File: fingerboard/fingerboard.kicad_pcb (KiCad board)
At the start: 2 copper layers, 15 x 75.5 mm, 8 parts, among them J1 Conn_01x05_Pin, SW1 SW_Push, SW2 SW_Push, SW3 SW_Push, SW4 SW_Push

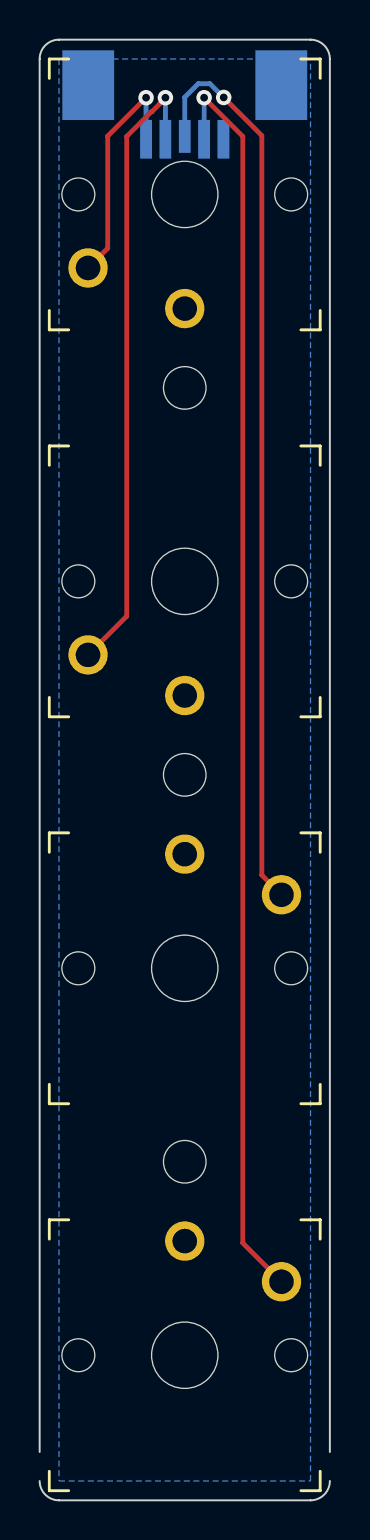
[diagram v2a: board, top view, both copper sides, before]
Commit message: tweak fingerboard more, incl new pinout
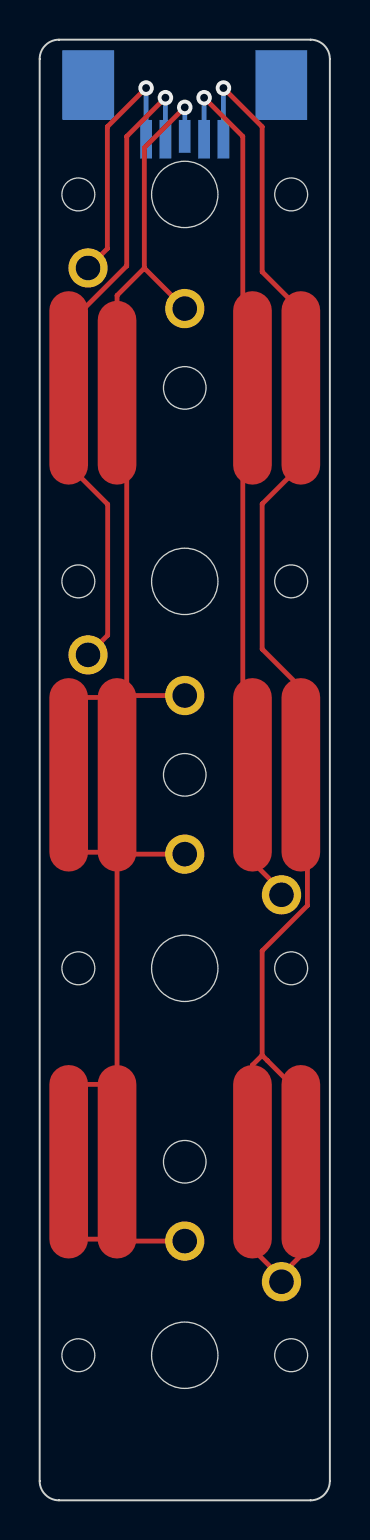
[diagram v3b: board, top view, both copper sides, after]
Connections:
- J1 pad 3: Row3 -> Column
- J1 pad 4: Row4 -> Row3
- J1 pad 5: Column -> Row4
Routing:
- net Column: track 0.00 -> 101.4 mm, vias 0 -> 1
- net Row4: track 65.0 -> 82.8 mm
- net Row2: track 32.6 -> 34.7 mm
- net Row3: track 47.2 -> 45.4 mm
- net Row1: track 12.2 -> 13.2 mm
- removed copper zone on B.Cu, net Column
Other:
- outline, holes or cut-outs redrawn
- board text added: "THIS SIDE DOWN"

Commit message: various tweaks, about to start on the carapace
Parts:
- J1: footprint Connector_FFC-FPC:TE_84952-5_1x05-1MP_P1.0mm_Horizontal -> panelization:FFC clamp fit 1x05 1.00mm
- moved J1 0.35 mm to (157.5, 35.0), turned to 180 degrees
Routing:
- net Row4: track 82.8 -> 80.1 mm
- net Row1: track 13.2 -> 10.5 mm
- net Row3: track 45.4 -> 43.8 mm
- net Row2: track 34.7 -> 33.0 mm
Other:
- board size 15 x 75.5 mm -> 15 x 74.5 mm
- board text added: "HER"
- board text added: "N"
- board text removed: "THIS SIDE DOWN"
